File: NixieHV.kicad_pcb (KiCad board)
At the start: 2 copper layers, 57.1 x 53.3 mm, 20 parts, among them P1 J1, P2 J2, P3 J3, Q1 IRF644PBF, U1 MAX1771_IC, U2 MCP41050

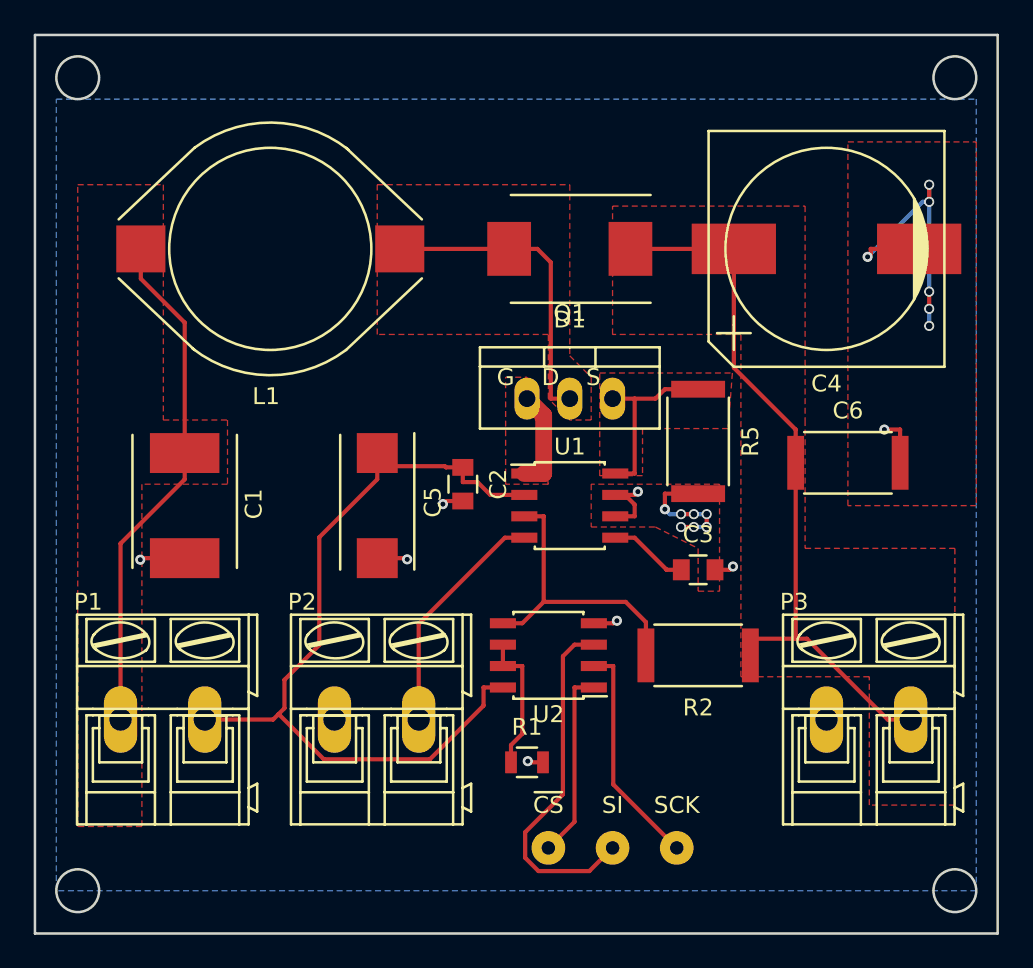
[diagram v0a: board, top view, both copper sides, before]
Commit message: Remove unnecessary files and copy parts to wheelerlab library
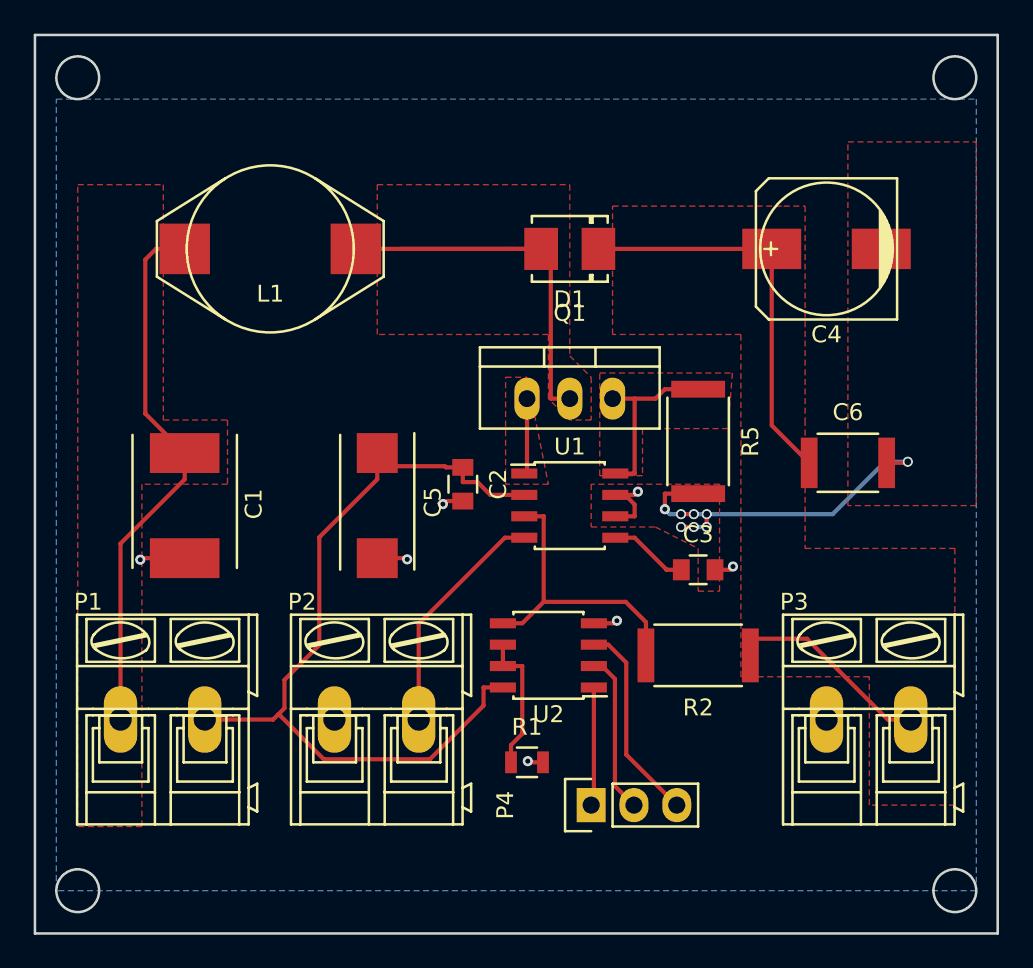
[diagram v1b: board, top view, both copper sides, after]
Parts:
- removed SCK, SI, ~CS: CONN_01X01, Wire_Pads:SolderWirePad_single_0-8mmDrill
- added P4: CONN_01X03, Pin_Headers:Pin_Header_Straight_1x03, F.Cu at (143.5, 133.3)
- C4: footprint TomsLibrary:C_SMD_12mm -> Capacitors_SMD:c_elec_8x10.5
- C6: footprint Resistors_SMD:R_2512 -> Capacitors_SMD:C_1812
- D1: footprint Diodes_SMD:DO-214AB -> Diodes_SMD:DO-214BA
- L1: footprint TomsLibrary:Inductor_18.54x15.24 -> Inductors:self_cms_we-pd3
- Q1: footprint Transistors_TO-220:TO-220_FET-GDS_Vertical -> TO_SOT_Packages_THT:TO-220_Neutral123_Vertical
- U1: value MAX1771_IC -> MAX1771
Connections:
- R5 pad 1: Net-(Q1-PadS) -> Net-(Q1-Pad3)
- U1 pad 1: Net-(Q1-PadG) -> Net-(Q1-Pad1)
- U1 pad 8: Net-(Q1-PadS) -> Net-(Q1-Pad3)
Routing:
- net Net-(D1-Pad2): track 18.5 -> 29.5 mm
- net Net-(Q1-PadS): track 10.9 -> 0.00 mm
- net Net-(Q1-Pad3): track 0.00 -> 10.9 mm
- net Net-(P4-Pad3): track 21.1 -> 12.1 mm
- net Net-(C4-Pad1): track 43.3 -> 36.4 mm
- net Net-(Q1-PadG): track 6.01 -> 0.00 mm
- net GNDD: track 41.9 -> 35.9 mm, vias 21 -> 15
- net Net-(Q1-Pad1): track 0.00 -> 4.51 mm
- net Net-(P4-Pad1): track 11.3 -> 7.07 mm
- net Net-(P4-Pad2): track 13.5 -> 10.1 mm
- net Net-(C1-Pad1): track 30.6 -> 32.5 mm
- added copper zone on F.Cu, net Net-(Q1-Pad1)
- added copper zone on F.Cu, net Net-(Q1-Pad3)
- removed copper zone on F.Cu, net Net-(Q1-PadG)
- removed copper zone on F.Cu, net Net-(Q1-PadS)
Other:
- net class ThickWidth removed
